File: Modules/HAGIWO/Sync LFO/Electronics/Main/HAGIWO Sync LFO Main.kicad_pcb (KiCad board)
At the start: 2 copper layers, 29.2 x 101.6 mm, 51 parts, among them J1 UP Out, J2 CLK In, J3 BP Inv, J4 BP Out, J5 Power, P1 B100K, P2 B100K, P3 B100K, P4 B100K, U1 TL072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

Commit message: KiCad 6 Update
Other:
- net class Default removed

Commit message: Update Sync LFO
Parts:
- moved A1 41.0 mm to (22.2, 29.2), turned to 180 degrees
- moved R5 26.7 mm to (14.6, 61.0), turned to 90 degrees
- moved C2 5.08 mm to (13.3, 22.9), turned to 90 degrees
- moved C3 5.08 mm to (13.3, 41.3), turned to 90 degrees
- moved R2 5.08 mm to (14.6, 22.9), turned to 90 degrees
- moved R3 5.08 mm to (14.6, 41.3), turned to 90 degrees
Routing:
- net +12V: track 97.6 -> 130.7 mm, vias 2 -> 4
- net D3: track 39.3 -> 66.5 mm
- net D10: track 60.4 -> 43.8 mm
- net A5: track 29.3 -> 45.8 mm
- net A0: track 30.3 -> 41.4 mm, vias 0 -> 2
- net Net-(C5-Pad2): track 55.3 -> 44.4 mm
- net A1: track 14.1 -> 20.4 mm, vias 0 -> 2
- net +5V: track 99.0 -> 104.1 mm
- net A3: track 15.6 -> 12.6 mm
- net GND: vias 7 -> 5
- net -12V: vias 5 -> 4
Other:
- board text added: "HAGIWO Sync LFO Main Rev. 022303"
- board text removed: "HAGIWO Sync LFO Main Rev. 012202"

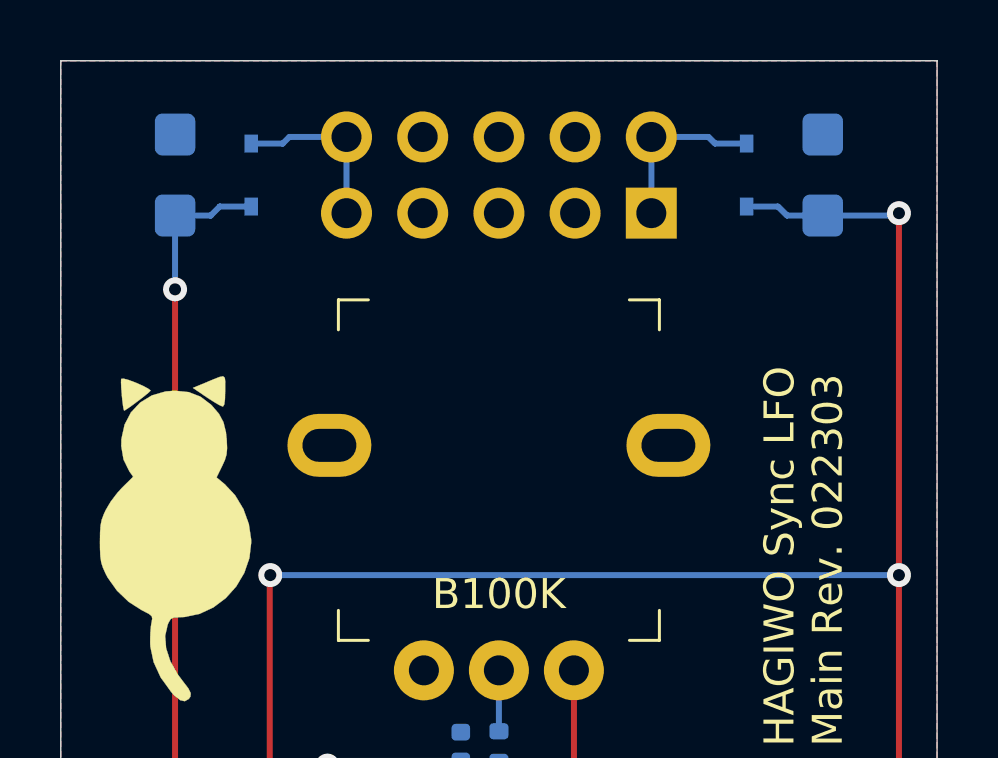
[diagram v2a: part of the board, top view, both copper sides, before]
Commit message: Add files via upload
Move components for shrouded IDC header. Add Silkscreen for USB Connector
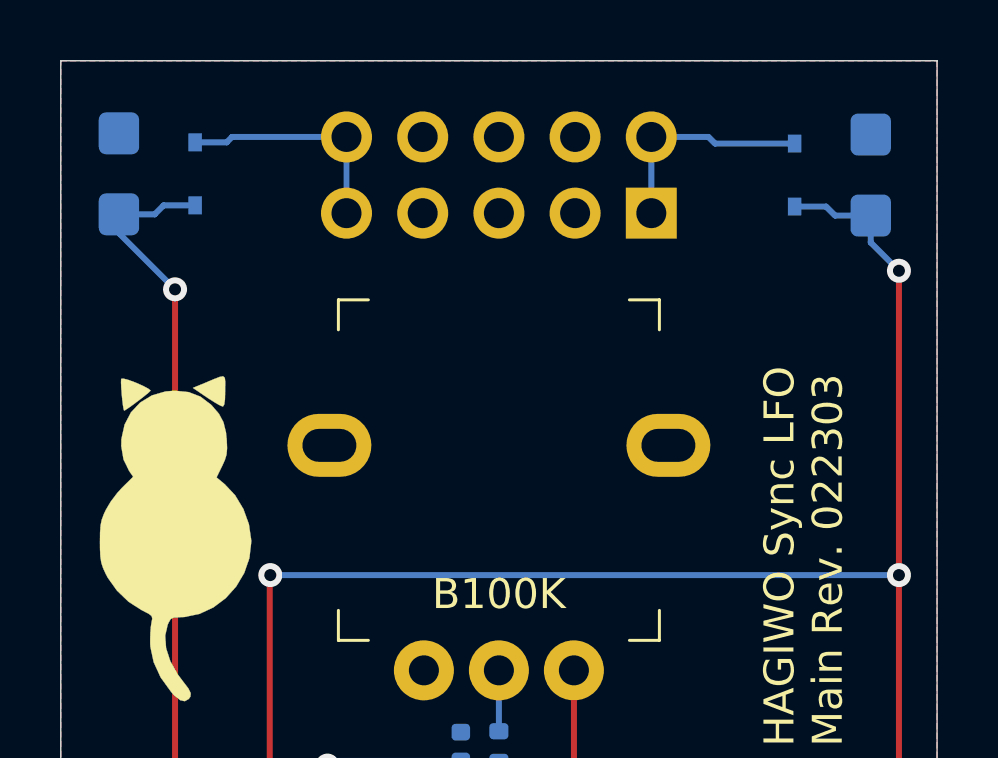
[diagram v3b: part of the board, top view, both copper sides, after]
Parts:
- moved C11 1.87 mm to (1.94, 3.77)
- moved D4 1.87 mm to (4.48, 3.77)
- moved C8 1.60 mm to (27.0, 3.81)
- moved D3 1.60 mm to (24.5, 3.81)
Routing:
- net +12V: track 130.7 -> 128.4 mm
- net Net-(D4-Pad1): track 5.81 -> 7.66 mm
- net Net-(D3-Pad2): track 5.81 -> 7.41 mm
- net -12V: track 109.1 -> 109.9 mm
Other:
- board text added: "USB HERE"
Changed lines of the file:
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@@
   )
   (footprint "Capacitor_Tantalum_SMD:CP_EIA-3216-18_Kemet-A" (layer "B.Cu")
-    (at 25.4 3.81 90)
+    (at 27 3.81 90)
     (descr "Tantalum Capacitor SMD Kemet-A (3216-18 Metric), IPC_7351 nominal, (Body size from: http://www.kemet.com/Lists/ProductCatalog/Attachments/253/KEM_TC101_STD.pdf), generated with kicad-footprint-generator")
     (tags "capacitor tantalum")
@@
   )
   (footprint "Capacitor_Tantalum_SMD:CP_EIA-3216-18_Kemet-A" (layer "B.Cu")
-    (at 3.81 3.81 -90)
+    (at 1.94 3.77 -90)
     (descr "Tantalum Capacitor SMD Kemet-A (3216-18 Metric), IPC_7351 nominal, (Body size from: http://www.kemet.com/Lists/ProductCatalog/Attachments/253/KEM_TC101_STD.pdf), generated with kicad-footprint-generator")
     (tags "capacitor tantalum")
@@
   )
   (footprint "Diode_SMD:D_SOD-323" (layer "B.Cu")
-    (at 22.86 3.81 90)
+    (at 24.46 3.81 90)
     (descr "SOD-323")
     (tags "SOD-323")
@@
   )
   (footprint "Diode_SMD:D_SOD-323" (layer "B.Cu")
-    (at 6.35 3.81 -90)
+    (at 4.48 3.77 -90)
     (descr "SOD-323")
     (tags "SOD-323")
@@
   (gr_line (start 29.21 101.6) (end 0 101.6) (layer "Edge.Cuts") (width 0.05))
   (gr_line (start 0 0) (end 29.21 0) (layer "Edge.Cuts") (width 0.05))
+  (gr_text "USB\nHERE" (at 14.585 68.5) (layer "B.SilkS")
+    (effects (font (size 1.5 1.5) (thickness 0.3)) (justify mirror))
+  )
   (gr_text "HAGIWO Sync LFO\nMain Rev. 022303" (at 24.765 22.86 90) (layer "F.SilkS")
     (effects (font (size 1 1) (thickness 0.1)) (justify left))
   )
-  (segment (start 27.94 5.08) (end 27.94 5.08) (width 0.2) (layer "F.Cu") (net 1))
   (segment (start 6.985 17.145) (end 6.965 17.165) (width 0.2) (layer "F.Cu") (net 1))
-  (segment (start 27.94 17.145) (end 27.94 5.08) (width 0.2) (layer "F.Cu") (net 1))
   (segment (start 6.965 17.165) (end 6.965 29.21) (width 0.2) (layer "F.Cu") (net 1))
   (segment (start 27.94 67.31) (end 27.94 17.145) (width 0.2) (layer "F.Cu") (net 1))
-  (via (at 27.94 5.08) (size 0.8) (drill 0.4) (layers "F.Cu" "B.Cu") (net 1))
+  (segment (start 27.94 17.145) (end 27.94 7) (width 0.2) (layer "F.Cu") (net 1))
+  (via (at 27.94 7) (size 0.8) (drill 0.4) (layers "F.Cu" "B.Cu") (net 1))
   (via (at 27.94 17.145) (size 0.8) (drill 0.4) (layers "F.Cu" "B.Cu") (net 1))
   (via (at 27.94 67.31) (size 0.8) (drill 0.4) (layers "F.Cu" "B.Cu") (net 1))
@@
   (segment (start 10.16 67.31) (end 22.225 67.31) (width 0.2) (layer "B.Cu") (net 1))
   (segment (start 7.775 69.695) (end 10.16 67.31) (width 0.2) (layer "B.Cu") (net 1))
-  (segment (start 25.4 5.16) (end 27.86 5.16) (width 0.2) (layer "B.Cu") (net 1))
   (segment (start 27.94 69.215) (end 27.94 67.31) (width 0.2) (layer "B.Cu") (net 1))
   (segment (start 7.62 70.005) (end 7.775 69.85) (width 0.2) (layer "B.Cu") (net 1))
   (segment (start 22.225 67.31) (end 27.94 67.31) (width 0.2) (layer "B.Cu") (net 1))
-  (segment (start 27.86 5.16) (end 27.94 5.08) (width 0.2) (layer "B.Cu") (net 1))
-  (segment (start 22.86 4.86) (end 23.91 4.86) (width 0.2) (layer "B.Cu") (net 1))
+  (segment (start 24.46 4.86) (end 25.51 4.86) (width 0.2) (layer "B.Cu") (net 1))
   (segment (start 25.4 71.82) (end 25.4 69.695) (width 0.2) (layer "B.Cu") (net 1))
-  (segment (start 24.21 5.16) (end 25.4 5.16) (width 0.2) (layer "B.Cu") (net 1))
+  (segment (start 25.81 5.16) (end 27 5.16) (width 0.2) (layer "B.Cu") (net 1))
   (segment (start 7.775 69.85) (end 7.775 69.695) (width 0.2) (layer "B.Cu") (net 1))
-  (segment (start 23.91 4.86) (end 24.21 5.16) (width 0.2) (layer "B.Cu") (net 1))
+  (segment (start 25.51 4.86) (end 25.81 5.16) (width 0.2) (layer "B.Cu") (net 1))
   (segment (start 7.62 71.885) (end 7.62 70.005) (width 0.2) (layer "B.Cu") (net 1))
   (segment (start 27.46 69.695) (end 27.94 69.215) (width 0.2) (layer "B.Cu") (net 1))
+  (segment (start 27 6.06) (end 27.94 7) (width 0.2) (layer "B.Cu") (net 1))
   (segment (start 27.94 17.145) (end 6.985 17.145) (width 0.2) (layer "B.Cu") (net 1))
+  (segment (start 27 5.16) (end 27 6.06) (width 0.2) (layer "B.Cu") (net 1))
   (segment (start 25.4 69.695) (end 27.46 69.695) (width 0.2) (layer "B.Cu") (net 1))
   (via (at 27.305 78.74) (size 0.8) (drill 0.4) (layers "F.Cu" "B.Cu") (net 2))
@@
   (segment (start 3.81 65.405) (end 3.81 65.405) (width 0.2) (layer "B.Cu") (net 13))
   (segment (start 20.32 63.5) (end 20.32 63.5) (width 0.2) (layer "B.Cu") (net 13))
-  (segment (start 3.81 7.62) (end 3.81 5.16) (width 0.2) (layer "B.Cu") (net 13))
   (segment (start 3.81 63.5) (end 3.81 65.405) (width 0.2) (layer "B.Cu") (net 13))
-  (segment (start 3.81 5.16) (end 5 5.16) (width 0.2) (layer "B.Cu") (net 13))
+  (segment (start 1.94 5.12) (end 3.13 5.12) (width 0.2) (layer "B.Cu") (net 13))
   (segment (start 2.385 66.83) (end 3.81 65.405) (width 0.2) (layer "B.Cu") (net 13))
   (segment (start 2.385 76.835) (end 2.385 66.83) (width 0.2) (layer "B.Cu") (net 13))
-  (segment (start 5 5.16) (end 5.3 4.86) (width 0.2) (layer "B.Cu") (net 13))
+  (segment (start 3.13 5.12) (end 3.43 4.82) (width 0.2) (layer "B.Cu") (net 13))
   (segment (start 2.385 76.835) (end 3.81 76.835) (width 0.2) (layer "B.Cu") (net 13))
   (segment (start 21.59 76.77) (end 21.59 78.585) (width 0.2) (layer "B.Cu") (net 13))
   (segment (start 21.59 78.585) (end 21.745 78.74) (width 0.2) (layer "B.Cu") (net 13))
-  (segment (start 5.3 4.86) (end 6.35 4.86) (width 0.2) (layer "B.Cu") (net 13))
+  (segment (start 3.81 7.62) (end 1.94 5.75) (width 0.2) (layer "B.Cu") (net 13))
+  (segment (start 3.43 4.82) (end 4.48 4.82) (width 0.2) (layer "B.Cu") (net 13))
+  (segment (start 1.94 5.75) (end 1.94 5.12) (width 0.2) (layer "B.Cu") (net 13))
   (segment (start 3.81 63.5) (end 20.32 63.5) (width 0.2) (layer "B.Cu") (net 13))
   (segment (start 20.89 76.77) (end 20.32 76.2) (width 0.2) (layer "B.Cu") (net 13))
@@
   (segment (start 15.875 89.535) (end 15.875 90.805) (width 0.2) (layer "B.Cu") (net 14))
   (segment (start 19.685 2.54) (end 21.59 2.54) (width 0.2) (layer "B.Cu") (net 15))
-  (segment (start 21.81 2.76) (end 21.59 2.54) (width 0.2) (layer "B.Cu") (net 15))
-  (segment (start 22.86 2.76) (end 21.81 2.76) (width 0.2) (layer "B.Cu") (net 15))
   (segment (start 19.685 2.54) (end 19.685 5.08) (width 0.2) (layer "B.Cu") (net 15))
-  (segment (start 9.525 2.54) (end 7.62 2.54) (width 0.2) (layer "B.Cu") (net 16))
+  (segment (start 21.59 2.54) (end 21.81 2.76) (width 0.2) (layer "B.Cu") (net 15))
+  (segment (start 21.81 2.76) (end 24.46 2.76) (width 0.2) (layer "B.Cu") (net 15))
+  (segment (start 5.71 2.54) (end 5.53 2.72) (width 0.2) (layer "B.Cu") (net 16))
+  (segment (start 9.525 2.54) (end 5.71 2.54) (width 0.2) (layer "B.Cu") (net 16))
+  (segment (start 5.53 2.72) (end 4.48 2.72) (width 0.2) (layer "B.Cu") (net 16))
   (segment (start 9.525 5.08) (end 9.525 2.54) (width 0.2) (layer "B.Cu") (net 16))
-  (segment (start 7.4 2.76) (end 7.62 2.54) (width 0.2) (layer "B.Cu") (net 16))
-  (segment (start 6.35 2.76) (end 7.4 2.76) (width 0.2) (layer "B.Cu") (net 16))
   (segment (start 1.43 96.52) (end 3.935 96.52) (width 0.2) (layer "B.Cu") (net 17))
   (segment (start 3.81 85.6) (end 3.05 85.6) (width 0.2) (layer "B.Cu") (net 18))
